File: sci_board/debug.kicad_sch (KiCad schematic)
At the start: 5 parts, among them J3 Conn_01x03_Pin, J4 Conn_01x03_Pin, J5 Conn_01x03_Pin

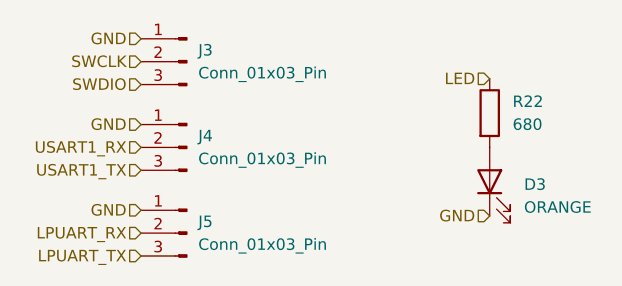
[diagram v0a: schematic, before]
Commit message: begin to update the pcb
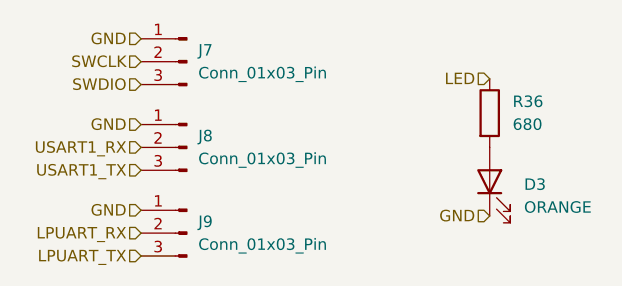
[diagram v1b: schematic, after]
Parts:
- renumbered J3 to J7, J4 to J8, J5 to J9, R22 to R36
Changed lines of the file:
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@@
 		(dnp no)
 		(fields_autoplaced yes)
-		(property "Reference" "J3"
+		(property "Reference" "J7"
 			(at 36.195 17.1449 0)
 			(effects
@@
 			(project ""
 				(path "/b4b2c88d-f6cd-4e60-862d-e21f68728580/840799ac-4fe6-4a8e-96a2-299affeec8e4/f58571f8-7a23-4346-b543-1a252fc91f18"
-					(reference "J3")
+					(reference "J7")
 					(unit 1)
 				)
@@
 		(dnp no)
 		(fields_autoplaced yes)
-		(property "Reference" "J5"
+		(property "Reference" "J9"
 			(at 36.195 36.1949 0)
 			(effects
@@
 			(project "sci_board"
 				(path "/b4b2c88d-f6cd-4e60-862d-e21f68728580/840799ac-4fe6-4a8e-96a2-299affeec8e4/f58571f8-7a23-4346-b543-1a252fc91f18"
-					(reference "J5")
+					(reference "J9")
 					(unit 1)
 				)
@@
 		(dnp no)
 		(fields_autoplaced yes)
-		(property "Reference" "J4"
+		(property "Reference" "J8"
 			(at 36.195 26.6699 0)
 			(effects
@@
 			(project "sci_board"
 				(path "/b4b2c88d-f6cd-4e60-862d-e21f68728580/840799ac-4fe6-4a8e-96a2-299affeec8e4/f58571f8-7a23-4346-b543-1a252fc91f18"
-					(reference "J4")
+					(reference "J8")
 					(unit 1)
 				)
@@
 		(dnp no)
 		(fields_autoplaced yes)
-		(property "Reference" "R22"
+		(property "Reference" "R36"
 			(at 71.12 22.8599 0)
 			(effects
@@
 			(project ""
 				(path "/b4b2c88d-f6cd-4e60-862d-e21f68728580/840799ac-4fe6-4a8e-96a2-299affeec8e4/f58571f8-7a23-4346-b543-1a252fc91f18"
-					(reference "R22")
-					(unit 1)
-				)
+					(reference "R36")
+					(unit 1)
+				)

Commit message: changed over SCI to smaller footprint switches
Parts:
- removed D3: ORANGE, LED_SMD:LED_0603_1608Metric_Pad1.05x0.95mm_HandSolder, symbol Device:LED
- removed R36: 680, Resistor_SMD:R_0603_1608Metric_Pad0.98x0.95mm_HandSolder, symbol Device:R
- added D4: LED_SMD_RED, LED_SMD:LED_0603_1608Metric_Pad1.05x0.95mm_HandSolder, symbol Device:LED
- added D5: LED_SMD_GREEN, LED_SMD:LED_0603_1608Metric_Pad1.05x0.95mm_HandSolder, symbol Device:LED
- added D6, D7, D8: LED_SMD_YELLOW, LED_SMD:LED_0603_1608Metric_Pad1.05x0.95mm_HandSolder, symbol Device:LED
- added R40, R41, R42, R43, R44: 680, Resistor_SMD:R_0402_1005Metric_Pad0.72x0.64mm_HandSolder, symbol Device:R
- renumbered J9 to J10, J7 to J8, J8 to J9
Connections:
- net GND: now also D4.1 (K), D5.1 (K), D6.1 (K), D7.1 (K), D8.1 (K)
- new net: D7.2 (A), R43.1
- new net: D8.2 (A), R44.1
- new net: D5.2 (A), R41.1
- new net: D4.2 (A), R40.1
- new net: D6.2 (A), R42.1
- new net LED_GPIO1: R40.2
- new net LED_GPIO2: R41.2
- new net LED_GPIO3: R42.2
- new net LED_GPIO4: R43.2
- new net LED_GPIO5: R44.2
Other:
- moved on the sheet: J10, J8, J9

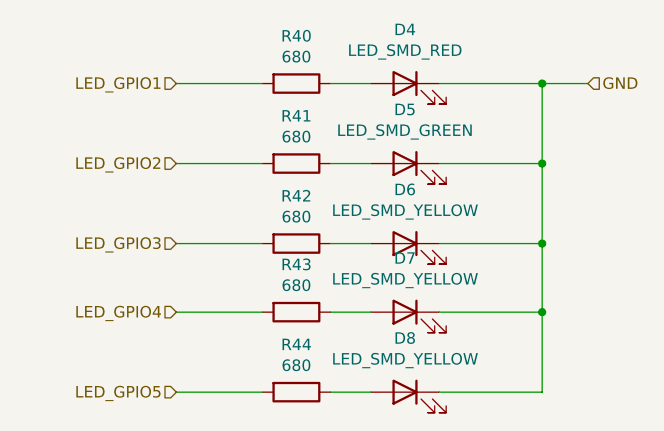
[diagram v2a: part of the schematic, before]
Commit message: replace nearly all buck converters with boost buck (missing is 5raw
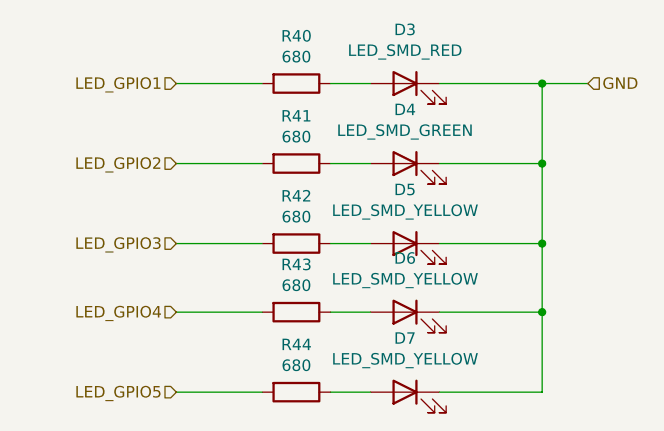
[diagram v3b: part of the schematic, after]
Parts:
- renumbered D4 to D3, D5 to D4, D6 to D5, D7 to D6, D8 to D7
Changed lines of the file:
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@@
 		(on_board yes)
 		(dnp no)
-		(property "Reference" "D7"
+		(property "Reference" "D6"
 			(at 133.35 60.071 0)
 			(effects
@@
 			(project "sci_board"
 				(path "/b4b2c88d-f6cd-4e60-862d-e21f68728580/840799ac-4fe6-4a8e-96a2-299affeec8e4/f58571f8-7a23-4346-b543-1a252fc91f18"
-					(reference "D7")
+					(reference "D6")
 					(unit 1)
 				)
@@
 		(on_board yes)
 		(dnp no)
-		(property "Reference" "D8"
+		(property "Reference" "D7"
 			(at 133.35 68.961 0)
 			(effects
@@
 			(project "sci_board"
 				(path "/b4b2c88d-f6cd-4e60-862d-e21f68728580/840799ac-4fe6-4a8e-96a2-299affeec8e4/f58571f8-7a23-4346-b543-1a252fc91f18"
-					(reference "D8")
+					(reference "D7")
 					(unit 1)
 				)
@@
 		(on_board yes)
 		(dnp no)
-		(property "Reference" "D4"
+		(property "Reference" "D3"
 			(at 133.35 34.671 0)
 			(effects
@@
 			(project "sci_board"
 				(path "/b4b2c88d-f6cd-4e60-862d-e21f68728580/840799ac-4fe6-4a8e-96a2-299affeec8e4/f58571f8-7a23-4346-b543-1a252fc91f18"
-					(reference "D4")
+					(reference "D3")
 					(unit 1)
 				)
@@
 		(on_board yes)
 		(dnp no)
-		(property "Reference" "D5"
+		(property "Reference" "D4"
 			(at 133.35 43.561 0)
 			(effects
@@
 			(project "sci_board"
 				(path "/b4b2c88d-f6cd-4e60-862d-e21f68728580/840799ac-4fe6-4a8e-96a2-299affeec8e4/f58571f8-7a23-4346-b543-1a252fc91f18"
-					(reference "D5")
+					(reference "D4")
 					(unit 1)
 				)
@@
 		(on_board yes)
 		(dnp no)
-		(property "Reference" "D6"
+		(property "Reference" "D5"
 			(at 133.35 52.451 0)
 			(effects
@@
 			(project "sci_board"
 				(path "/b4b2c88d-f6cd-4e60-862d-e21f68728580/840799ac-4fe6-4a8e-96a2-299affeec8e4/f58571f8-7a23-4346-b543-1a252fc91f18"
-					(reference "D6")
-					(unit 1)
-				)
+					(reference "D5")
+					(unit 1)
+				)

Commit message: temporary branch for radio to pc104
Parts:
- renumbered D3 to D5, D4 to D6, D5 to D7, D6 to D8, D7 to D9, J8 to J10, J9 to J11, J10 to J12, R40 to R28, R41 to R29, R42 to R30, R43 to R31, R44 to R32
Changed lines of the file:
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@@
 		(dnp no)
 		(fields_autoplaced yes)
-		(property "Reference" "J8"
+		(property "Reference" "J10"
 			(at 68.58 45.0849 0)
 			(effects
@@
 		)
 		(instances
+			(project ""
+				(path "/a863a5ec-a5d4-4f54-be53-e8c01d5e3ac4/53f12969-e593-459a-9671-cc23a5a9aea0/f4ff56ce-2fa2-4b99-a709-c113709260c1/730bd731-7be7-49ed-966d-7ccd975f4386"
+					(reference "J10")
+					(unit 1)
+				)
+			)
 			(project ""
 				(path "/b4b2c88d-f6cd-4e60-862d-e21f68728580/840799ac-4fe6-4a8e-96a2-299affeec8e4/f58571f8-7a23-4346-b543-1a252fc91f18"
@@
 		(on_board yes)
 		(dnp no)
-		(property "Reference" "D6"
+		(property "Reference" "D8"
 			(at 133.35 60.071 0)
 			(effects
@@
 		(instances
 			(project "sci_board"
+				(path "/a863a5ec-a5d4-4f54-be53-e8c01d5e3ac4/53f12969-e593-459a-9671-cc23a5a9aea0/f4ff56ce-2fa2-4b99-a709-c113709260c1/730bd731-7be7-49ed-966d-7ccd975f4386"
+					(reference "D8")
+					(unit 1)
+				)
+			)
+			(project "sci_board"
 				(path "/b4b2c88d-f6cd-4e60-862d-e21f68728580/840799ac-4fe6-4a8e-96a2-299affeec8e4/f58571f8-7a23-4346-b543-1a252fc91f18"
 					(reference "D6")
@@
 		(on_board yes)
 		(dnp no)
-		(property "Reference" "R43"
+		(property "Reference" "R31"
 			(at 121.285 60.7822 90)
 			(effects
@@
 		(instances
 			(project "sci_board"
+				(path "/a863a5ec-a5d4-4f54-be53-e8c01d5e3ac4/53f12969-e593-459a-9671-cc23a5a9aea0/f4ff56ce-2fa2-4b99-a709-c113709260c1/730bd731-7be7-49ed-966d-7ccd975f4386"
+					(reference "R31")
+					(unit 1)
+				)
+			)
+			(project "sci_board"
 				(path "/b4b2c88d-f6cd-4e60-862d-e21f68728580/840799ac-4fe6-4a8e-96a2-299affeec8e4/f58571f8-7a23-4346-b543-1a252fc91f18"
 					(reference "R43")
@@
 		(on_board yes)
 		(dnp no)
-		(property "Reference" "R44"
+		(property "Reference" "R32"
 			(at 121.285 69.6722 90)
 			(effects
@@
 		)
 		(instances
+			(project "sci_board"
+				(path "/a863a5ec-a5d4-4f54-be53-e8c01d5e3ac4/53f12969-e593-459a-9671-cc23a5a9aea0/f4ff56ce-2fa2-4b99-a709-c113709260c1/730bd731-7be7-49ed-966d-7ccd975f4386"
+					(reference "R32")
+					(unit 1)
+				)
+			)
 			(project "sci_board"
 				(path "/b4b2c88d-f6cd-4e60-862d-e21f68728580/840799ac-4fe6-4a8e-96a2-299affeec8e4/f58571f8-7a23-4346-b543-1a252fc91f18"
@@
 		(on_board yes)
 		(dnp no)
-		(property "Reference" "D7"
+		(property "Reference" "D9"
 			(at 133.35 68.961 0)
 			(effects
@@
 		(instances
 			(project "sci_board"
+				(path "/a863a5ec-a5d4-4f54-be53-e8c01d5e3ac4/53f12969-e593-459a-9671-cc23a5a9aea0/f4ff56ce-2fa2-4b99-a709-c113709260c1/730bd731-7be7-49ed-966d-7ccd975f4386"
+					(reference "D9")
+					(unit 1)
+				)
+			)
+			(project "sci_board"
 				(path "/b4b2c88d-f6cd-4e60-862d-e21f68728580/840799ac-4fe6-4a8e-96a2-299affeec8e4/f58571f8-7a23-4346-b543-1a252fc91f18"
 					(reference "D7")
@@
 		(on_board yes)
 		(dnp no)
-		(property "Reference" "R41"
+		(property "Reference" "R29"
 			(at 121.285 44.2722 90)
 			(effects
@@
 		)
 		(instances
+			(project "sci_board"
+				(path "/a863a5ec-a5d4-4f54-be53-e8c01d5e3ac4/53f12969-e593-459a-9671-cc23a5a9aea0/f4ff56ce-2fa2-4b99-a709-c113709260c1/730bd731-7be7-49ed-966d-7ccd975f4386"
+					(reference "R29")
+					(unit 1)
+				)
+			)
 			(project "sci_board"
 				(path "/b4b2c88d-f6cd-4e60-862d-e21f68728580/840799ac-4fe6-4a8e-96a2-299affeec8e4/f58571f8-7a23-4346-b543-1a252fc91f18"
@@
 		(on_board yes)
 		(dnp no)
-		(property "Reference" "D3"
+		(property "Reference" "D5"
 			(at 133.35 34.671 0)
 			(effects
@@
 		)
 		(instances
+			(project "sci_board"
+				(path "/a863a5ec-a5d4-4f54-be53-e8c01d5e3ac4/53f12969-e593-459a-9671-cc23a5a9aea0/f4ff56ce-2fa2-4b99-a709-c113709260c1/730bd731-7be7-49ed-966d-7ccd975f4386"
+					(reference "D5")
+					(unit 1)
+				)
+			)
 			(project "sci_board"
 				(path "/b4b2c88d-f6cd-4e60-862d-e21f68728580/840799ac-4fe6-4a8e-96a2-299affeec8e4/f58571f8-7a23-4346-b543-1a252fc91f18"
@@
 		(dnp no)
 		(fields_autoplaced yes)
-		(property "Reference" "J10"
+		(property "Reference" "J12"
 			(at 68.58 64.1349 0)
 			(effects
@@
 		(instances
 			(project "sci_board"
+				(path "/a863a5ec-a5d4-4f54-be53-e8c01d5e3ac4/53f12969-e593-459a-9671-cc23a5a9aea0/f4ff56ce-2fa2-4b99-a709-c113709260c1/730bd731-7be7-49ed-966d-7ccd975f4386"
+					(reference "J12")
+					(unit 1)
+				)
+			)
+			(project "sci_board"
 				(path "/b4b2c88d-f6cd-4e60-862d-e21f68728580/840799ac-4fe6-4a8e-96a2-299affeec8e4/f58571f8-7a23-4346-b543-1a252fc91f18"
 					(reference "J10")
@@
 		(on_board yes)
 		(dnp no)
-		(property "Reference" "R40"
+		(property "Reference" "R28"
 			(at 121.285 35.3822 90)
 			(effects
@@
 		)
 		(instances
+			(project "sci_board"
+				(path "/a863a5ec-a5d4-4f54-be53-e8c01d5e3ac4/53f12969-e593-459a-9671-cc23a5a9aea0/f4ff56ce-2fa2-4b99-a709-c113709260c1/730bd731-7be7-49ed-966d-7ccd975f4386"
+					(reference "R28")
+					(unit 1)
+				)
+			)
 			(project "sci_board"
 				(path "/b4b2c88d-f6cd-4e60-862d-e21f68728580/840799ac-4fe6-4a8e-96a2-299affeec8e4/f58571f8-7a23-4346-b543-1a252fc91f18"
@@
 		(dnp no)
 		(fields_autoplaced yes)
-		(property "Reference" "J9"
+		(property "Reference" "J11"
 			(at 68.58 54.6099 0)
 			(effects
@@
 		)
 		(instances
+			(project "sci_board"
+				(path "/a863a5ec-a5d4-4f54-be53-e8c01d5e3ac4/53f12969-e593-459a-9671-cc23a5a9aea0/f4ff56ce-2fa2-4b99-a709-c113709260c1/730bd731-7be7-49ed-966d-7ccd975f4386"
+					(reference "J11")
+					(unit 1)
+				)
+			)
 			(project "sci_board"
 				(path "/b4b2c88d-f6cd-4e60-862d-e21f68728580/840799ac-4fe6-4a8e-96a2-299affeec8e4/f58571f8-7a23-4346-b543-1a252fc91f18"
@@
 		(on_board yes)
 		(dnp no)
-		(property "Reference" "D4"
+		(property "Reference" "D6"
 			(at 133.35 43.561 0)
 			(effects
@@
 		)
 		(instances
+			(project "sci_board"
+				(path "/a863a5ec-a5d4-4f54-be53-e8c01d5e3ac4/53f12969-e593-459a-9671-cc23a5a9aea0/f4ff56ce-2fa2-4b99-a709-c113709260c1/730bd731-7be7-49ed-966d-7ccd975f4386"
+					(reference "D6")
+					(unit 1)
+				)
+			)
 			(project "sci_board"
 				(path "/b4b2c88d-f6cd-4e60-862d-e21f68728580/840799ac-4fe6-4a8e-96a2-299affeec8e4/f58571f8-7a23-4346-b543-1a252fc91f18"
@@
 		(on_board yes)
 		(dnp no)
-		(property "Reference" "D5"
+		(property "Reference" "D7"
 			(at 133.35 52.451 0)
 			(effects
@@
 		(instances
 			(project "sci_board"
+				(path "/a863a5ec-a5d4-4f54-be53-e8c01d5e3ac4/53f12969-e593-459a-9671-cc23a5a9aea0/f4ff56ce-2fa2-4b99-a709-c113709260c1/730bd731-7be7-49ed-966d-7ccd975f4386"
+					(reference "D7")
+					(unit 1)
+				)
+			)
+			(project "sci_board"
 				(path "/b4b2c88d-f6cd-4e60-862d-e21f68728580/840799ac-4fe6-4a8e-96a2-299affeec8e4/f58571f8-7a23-4346-b543-1a252fc91f18"
 					(reference "D5")
@@
 		(on_board yes)
 		(dnp no)
-		(property "Reference" "R42"
+		(property "Reference" "R30"
 			(at 121.285 53.1622 90)
 			(effects
@@
 		(instances
 			(project "sci_board"
-				(path "/b4b2c88d-f6cd-4e60-862d-e21f68728580/840799ac-4fe6-4a8e-96a2-299affeec8e4/f58571f8-7a23-4346-b543-1a252fc91f18"
+				(path "/a863a5ec-a5d4-4f54-be53-e8c01d5e3ac4/53f12969-e593-459a-9671-cc23a5a9aea0/f4ff56ce-2fa2-4b99-a709-c113709260c1/730bd731-7be7-49ed-966d-7ccd975f4386"
+					(reference "R30")
+					(unit 1)
+				)
+			)
+			(project "sci_board"
+				(path "/b4b2c88d-f6cd-4e60-862d-e21f68728580/840799ac-4fe6-4a8e-96a2-299affeec8e4/f58571f8-7a23-4346-b543-1a252fc91f18"
